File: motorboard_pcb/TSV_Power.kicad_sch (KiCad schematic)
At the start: 14 parts, among them J4 Screw_Terminal_01x02, U5 LM5012QDDARQ1

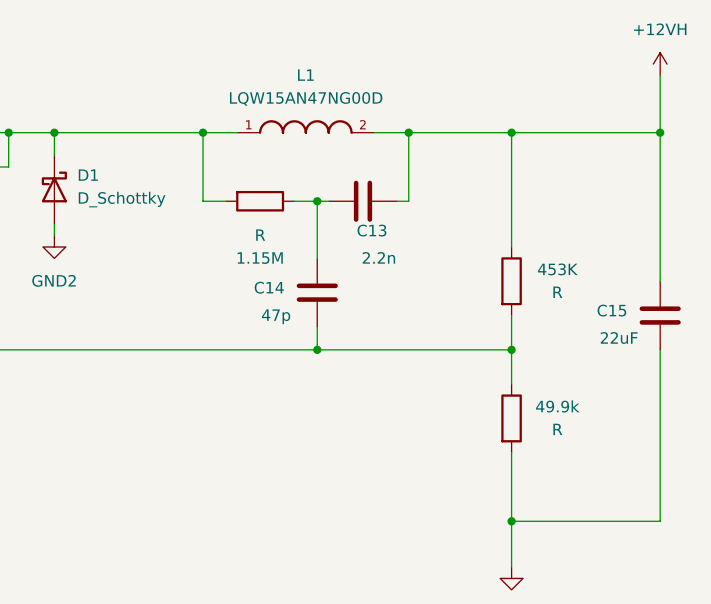
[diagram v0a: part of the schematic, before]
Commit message: switch isolator for SPI, output stage (DAC, op amp)
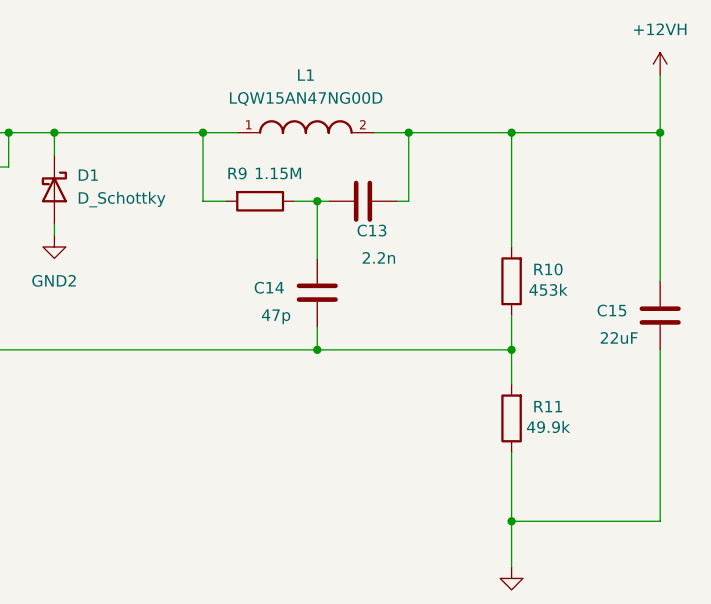
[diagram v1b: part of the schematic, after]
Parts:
- removed 1.15M, 453K, 49.9k: R, symbol Device:R
- added R10: 453k, symbol Device:R
- added R11: 49.9k, symbol Device:R
- added R9: 1.15M, symbol Device:R
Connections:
- net +12VH: now also R10.2
- net GND2: now also R11.1
- net at C12.2, D1.1 (K), L1.1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: now also R9.2
- net at C14.2, U5.5 (FB): now also R10.1, R11.2
- net at C13.1, C14.1: now also R9.1
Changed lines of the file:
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@@
+	)
+	(symbol
+		(lib_id "Device:R")
+		(at 207.01 58.42 270)
+		(unit 1)
+		(exclude_from_sim no)
+		(in_bom yes)
+		(on_board yes)
+		(dnp no)
+		(property "Reference" "R9"
+			(at 204.47 55.372 90)
+			(effects
+				(font
+					(size 1.27 1.27)
+				)
+			)
+		)
+		(property "Value" "1.15M"
+			(at 209.042 55.372 90)
+			(effects
+				(font
+					(size 1.27 1.27)
+				)
+			)
+		)
+		(property "Footprint" ""
+			(at 207.01 56.642 90)
+			(effects
+				(font
+					(size 1.27 1.27)
+				)
+				(hide yes)
+			)
+		)
+		(property "Datasheet" "~"
+			(at 207.01 58.42 0)
+			(effects
+				(font
+					(size 1.27 1.27)
+				)
+				(hide yes)
+			)
+		)
+		(property "Description" "Resistor"
+			(at 207.01 58.42 0)
+			(effects
+				(font
+					(size 1.27 1.27)
+				)
+				(hide yes)
+			)
+		)
+		(pin "2"
+		)
+		(pin "1"
+		)
+		(instances
+			(project "motorboard"
+				(path "/fa713205-4357-49d0-ad77-7aa2864b7782/664be53a-ecbc-49c3-915e-4aa63b1c21ee"
+					(reference "R9")
+					(unit 1)
+				)
+			)
+		)
 	)
 	(symbol
@@
 	(symbol
 		(lib_id "Device:R")
-		(at 234.95 67.31 0)
-		(unit 1)
-		(exclude_from_sim no)
-		(in_bom yes)
-		(on_board yes)
-		(dnp no)
-		(property "Reference" "453K"
-			(at 240.03 66.04 0)
-			(effects
-				(font
-					(size 1.27 1.27)
-				)
-			)
-		)
-		(property "Value" "R"
-			(at 240.03 68.58 0)
-			(effects
-				(font
-					(size 1.27 1.27)
-				)
-			)
-		)
-		(property "Footprint" ""
-			(at 233.172 67.31 90)
+		(at 234.95 82.55 180)
+		(unit 1)
+		(exclude_from_sim no)
+		(in_bom yes)
+		(on_board yes)
+		(dnp no)
+		(property "Reference" "R11"
+			(at 239.014 81.28 0)
+			(effects
+				(font
+					(size 1.27 1.27)
+				)
+			)
+		)
+		(property "Value" "49.9k"
+			(at 239.014 83.566 0)
+			(effects
+				(font
+					(size 1.27 1.27)
+				)
+			)
+		)
+		(property "Footprint" ""
+			(at 236.728 82.55 90)
 			(effects
 				(font
@@
 		)
 		(property "Datasheet" "~"
-			(at 234.95 67.31 0)
+			(at 234.95 82.55 0)
 			(effects
 				(font
@@
 		)
 		(property "Description" "Resistor"
-			(at 234.95 67.31 0)
+			(at 234.95 82.55 0)
 			(effects
 				(font
@@
 			(project "motorboard"
 				(path "/fa713205-4357-49d0-ad77-7aa2864b7782/664be53a-ecbc-49c3-915e-4aa63b1c21ee"
-					(reference "453K")
+					(reference "R11")
 					(unit 1)
 				)
@@
 	(symbol
 		(lib_id "Device:R")
-		(at 207.01 58.42 270)
-		(unit 1)
-		(exclude_from_sim no)
-		(in_bom yes)
-		(on_board yes)
-		(dnp no)
-		(property "Reference" "1.15M"
-			(at 207.01 64.77 90)
-			(effects
-				(font
-					(size 1.27 1.27)
-				)
-			)
-		)
-		(property "Value" "R"
-			(at 207.01 62.23 90)
-			(effects
-				(font
-					(size 1.27 1.27)
-				)
-			)
-		)
-		(property "Footprint" ""
-			(at 207.01 56.642 90)
-			(effects
-				(font
-					(size 1.27 1.27)
-				)
-				(hide yes)
-			)
-		)
-		(property "Datasheet" "~"
-			(at 207.01 58.42 0)
-			(effects
-				(font
-					(size 1.27 1.27)
-				)
-				(hide yes)
-			)
-		)
-		(property "Description" "Resistor"
-			(at 207.01 58.42 0)
-			(effects
-				(font
-					(size 1.27 1.27)
-				)
-				(hide yes)
-			)
-		)
-		(pin "2"
-		)
-		(pin "1"
-		)
-		(instances
-			(project ""
-				(path "/fa713205-4357-49d0-ad77-7aa2864b7782/664be53a-ecbc-49c3-915e-4aa63b1c21ee"
-					(reference "1.15M")
-					(unit 1)
-				)
-			)
-		)
-	)
-	(symbol
-		(lib_id "Device:R")
 		(at 106.68 63.5 0)
 		(unit 1)
@@
 	(symbol
 		(lib_id "Device:R")
-		(at 234.95 82.55 0)
-		(unit 1)
-		(exclude_from_sim no)
-		(in_bom yes)
-		(on_board yes)
-		(dnp no)
-		(property "Reference" "49.9k"
-			(at 240.03 81.28 0)
-			(effects
-				(font
-					(size 1.27 1.27)
-				)
-			)
-		)
-		(property "Value" "R"
-			(at 240.03 83.82 0)
-			(effects
-				(font
-					(size 1.27 1.27)
-				)
-			)
-		)
-		(property "Footprint" ""
-			(at 233.172 82.55 90)
+		(at 234.95 67.31 180)
+		(unit 1)
+		(exclude_from_sim no)
+		(in_bom yes)
+		(on_board yes)
+		(dnp no)
+		(property "Reference" "R10"
+			(at 239.014 66.04 0)
+			(effects
+				(font
+					(size 1.27 1.27)
+				)
+			)
+		)
+		(property "Value" "453k"
+			(at 239.014 68.326 0)
+			(effects
+				(font
+					(size 1.27 1.27)
+				)
+			)
+		)
+		(property "Footprint" ""
+			(at 236.728 67.31 90)
 			(effects
 				(font
@@
 		)
 		(property "Datasheet" "~"
-			(at 234.95 82.55 0)
+			(at 234.95 67.31 0)
 			(effects
 				(font
@@
 		)
 		(property "Description" "Resistor"
-			(at 234.95 82.55 0)
+			(at 234.95 67.31 0)
 			(effects
 				(font
@@
 			(project "motorboard"
 				(path "/fa713205-4357-49d0-ad77-7aa2864b7782/664be53a-ecbc-49c3-915e-4aa63b1c21ee"
-					(reference "49.9k")
-					(unit 1)
-				)
+					(reference "R10")
+					(unit 1)
+				)

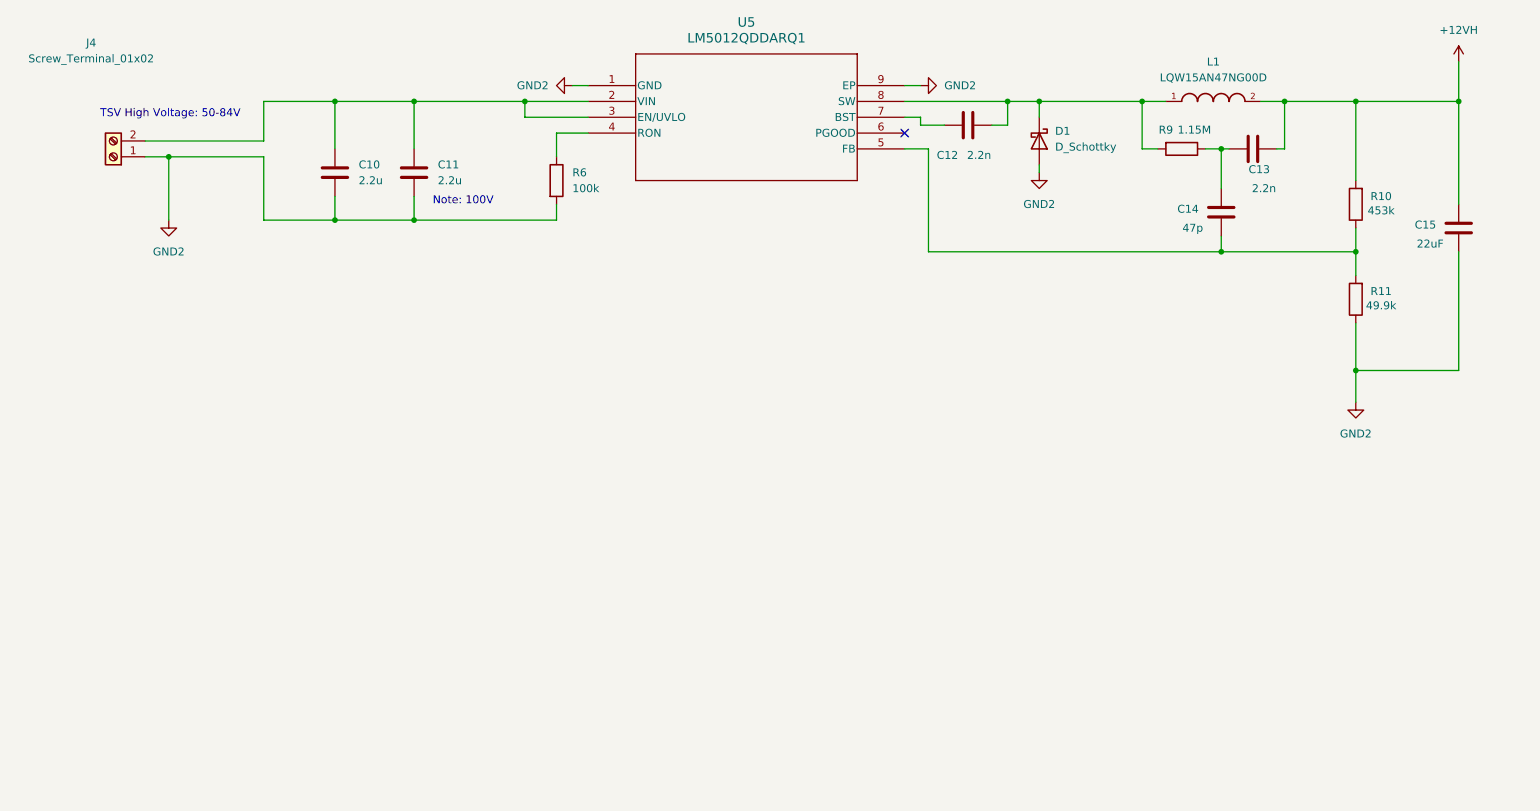
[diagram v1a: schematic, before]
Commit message: Schematic done, pending review
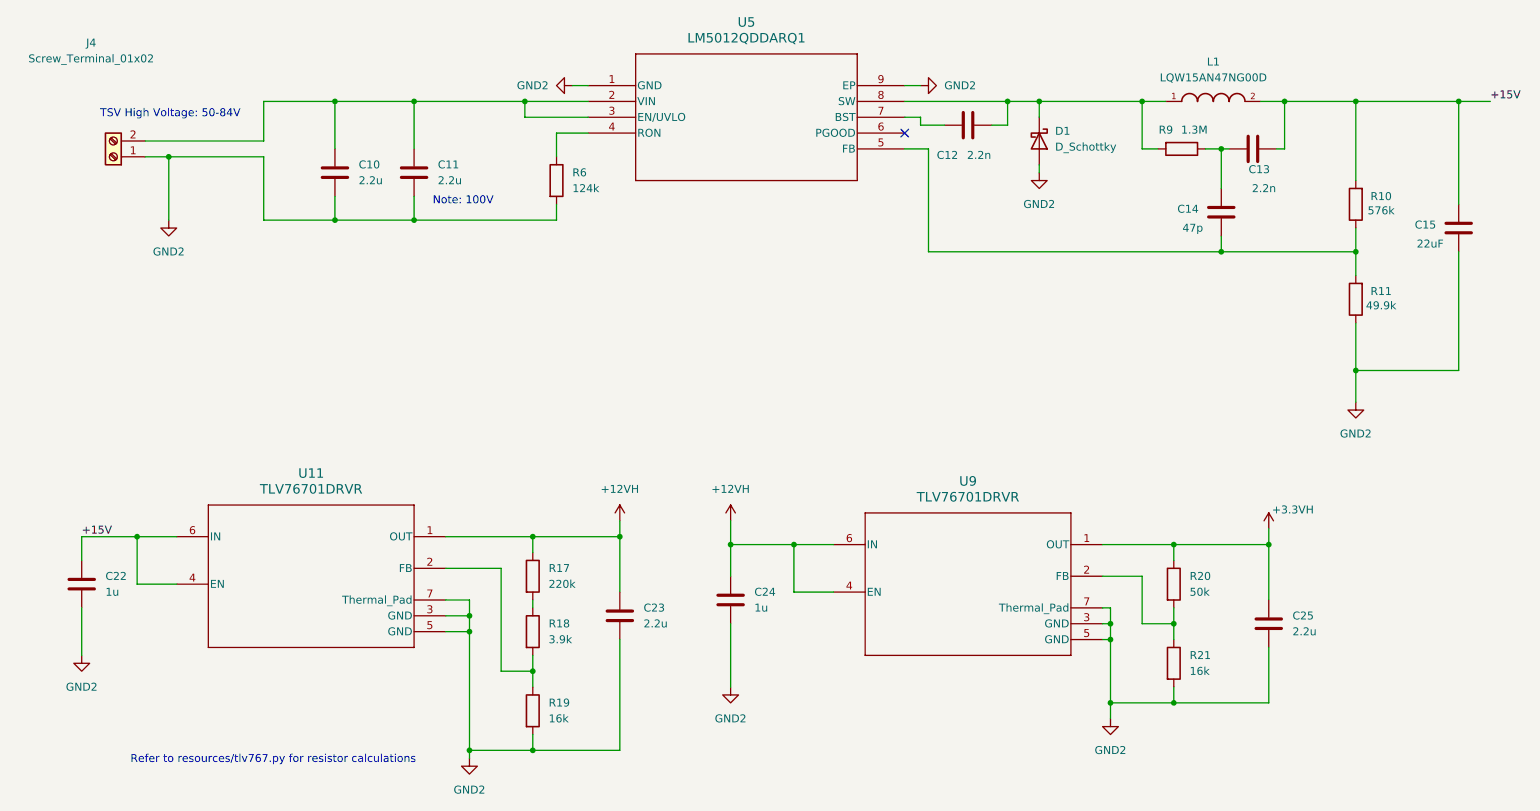
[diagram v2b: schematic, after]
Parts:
- added C22, C24: 1u, symbol Device:C
- added C23, C25: 2.2u, symbol Device:C
- added R17: 220k, symbol Device:R
- added R18: 3.9k, symbol Device:R
- added R19, R21: 16k, symbol Device:R
- added R20: 50k, symbol Device:R
- added U11, U9: TLV76701DRVR, TLV76701:DRV0006A-IPC_A, symbol TLV76701:TLV76701DRVR
- R10: value 453k -> 576k
- R6: value 100k -> 124k
- R9: value 1.15M -> 1.3M
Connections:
- net +12VH: now also C23.1, C24.1, R17.1, U11.1 (OUT), U9.4 (EN), U9.6 (IN); no longer C13.2, C15.1, L1.2, R10.2
- net GND2: now also C22.2, C23.2, C24.2, C25.2, R19.2, R21.2, U11.3 (GND), U11.5 (GND), U11.7 (Thermal_Pad), U9.3 (GND), U9.5 (GND), U9.7 (Thermal_Pad)
- new net: R17.2, R18.1
- new net: R18.2, R19.1, U11.2 (FB)
- new net: R20.2, R21.1, U9.2 (FB)
- new net +15V: C13.2, C15.1, C22.1, L1.2, R10.2, U11.4 (EN), U11.6 (IN)
- new net +3.3VH: C25.1, R20.1, U9.1 (OUT)
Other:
- note added: "Refer to resources/tlv767.py for resistor calculations"

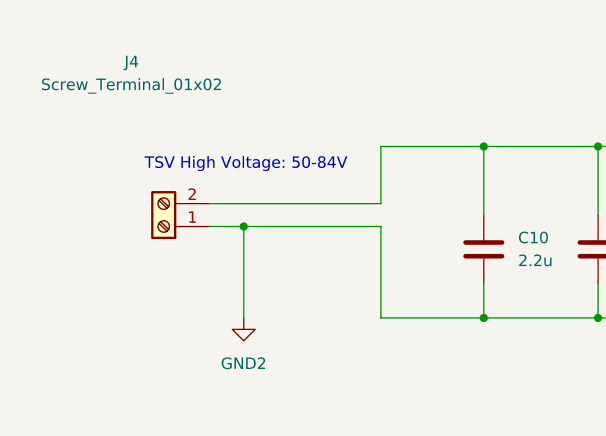
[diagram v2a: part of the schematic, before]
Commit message: Initial layout, all resistors/caps are 0602
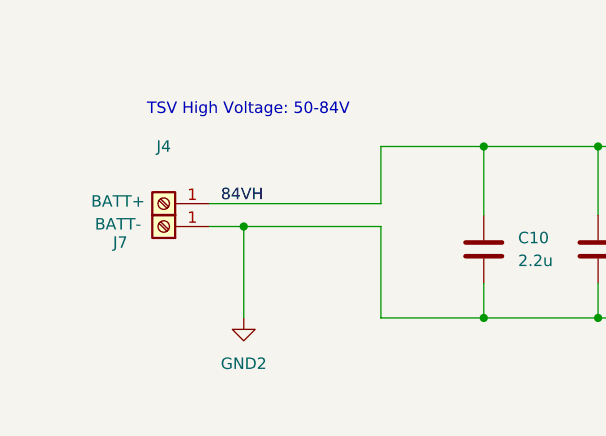
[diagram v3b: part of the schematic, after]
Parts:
- removed J4: Screw_Terminal_01x02, symbol Connector:Screw_Terminal_01x02
- added J4: BATT+, TerminalBlock_Wuerth:Wuerth_REDCUBE-THR_WP-THRBU_74650074_THR, symbol Connector:Screw_Terminal_01x01
- added J7: BATT-, TerminalBlock_Wuerth:Wuerth_REDCUBE-THR_WP-THRBU_74650074_THR, symbol Connector:Screw_Terminal_01x01
- C10, C11, C12, C13, C14, C15, C22, C23, C24, C25: footprint (none) -> Capacitor_SMD:C_0603_1608Metric
- D1: footprint (none) -> Diode_THT:D_DO-201AD_P15.24mm_Horizontal
- R10, R11, R17, R18, R19, R20, R21, R6, R9: footprint (none) -> Resistor_SMD:R_0603_1608Metric
- U5: footprint SO-8-DDA_TEX -> LM5201:SO-8-DDA_TEX
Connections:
- net GND2: now also J7.1 (Pin_1)
- net 84VH: now reaches C10.1, C11.1, U5.2 (VIN), U5.3 (EN/UVLO)
- net 84VH: now also J4.1 (Pin_1)

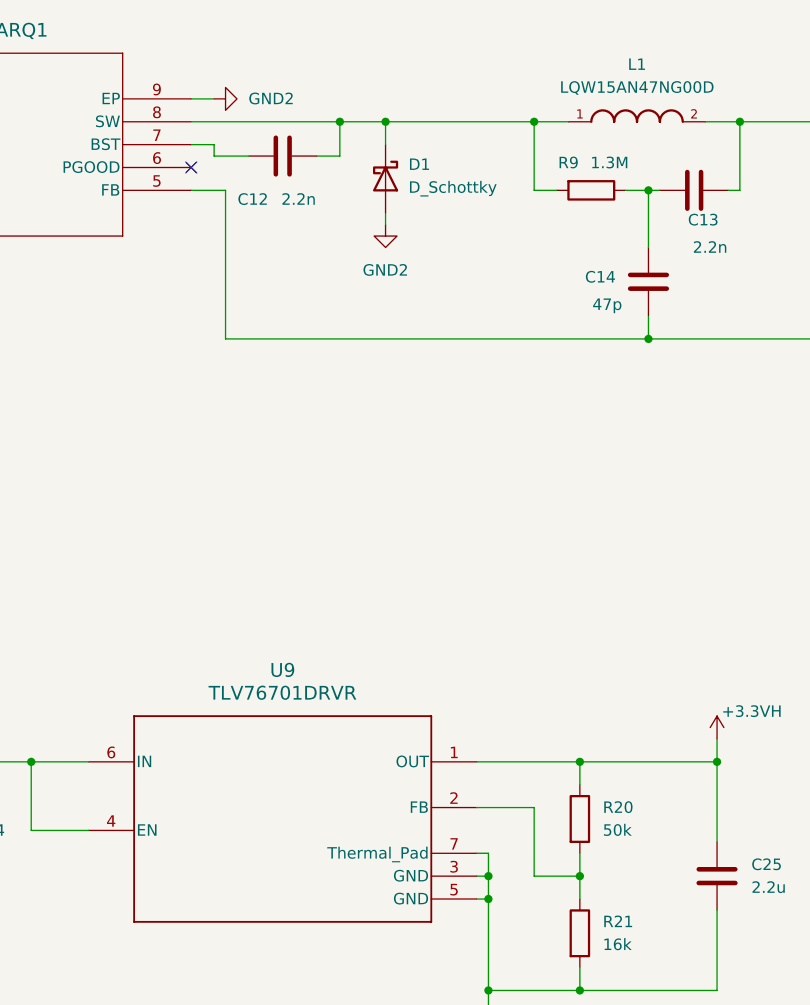
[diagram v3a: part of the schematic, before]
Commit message: layout finished, silkscreen finished, BOM finished
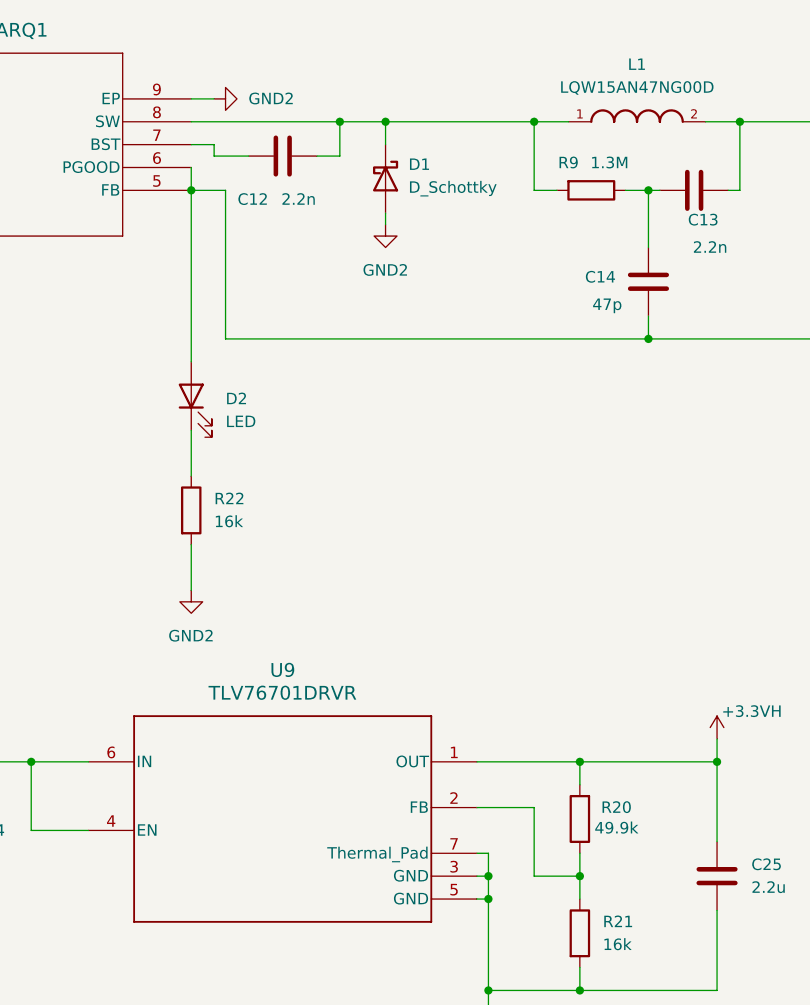
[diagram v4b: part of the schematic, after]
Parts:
- added D2: LED, LED_SMD:LED_0805_2012Metric, symbol Device:LED
- added R22: 16k, Resistor_SMD:R_0603_1608Metric, symbol Device:R
- C10, C11: footprint Capacitor_SMD:C_0603_1608Metric -> Capacitor_SMD:C_1210_3225Metric_Pad1.33x2.70mm_HandSolder
- C12, C13, C14: footprint Capacitor_SMD:C_0603_1608Metric -> Capacitor_SMD:C_0805_2012Metric
- C15: footprint Capacitor_SMD:C_0603_1608Metric -> Capacitor_SMD:C_1210_3225Metric
- R20: value 50k -> 49.9k
- R6: footprint Resistor_SMD:R_0603_1608Metric -> Resistor_SMD:R_0402_1005Metric
- R9: footprint Resistor_SMD:R_0603_1608Metric -> Resistor_SMD:R_0402_1005Metric_Pad0.72x0.64mm_HandSolder
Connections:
- net +3.3VH: now also R20.2; no longer R20.1
- net GND2: now also R22.2
- net at C14.2, R10.1, R11.2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: now also U5.6 (PGOOD), D2.2 (A)
- net at R21.1, U9.2 (FB): now also R20.1; no longer R20.2
- new net: D2.1 (K), R22.1
- no-connect marks 1 -> 0
